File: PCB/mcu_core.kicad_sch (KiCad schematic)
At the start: 24 parts, among them X1 12MHz

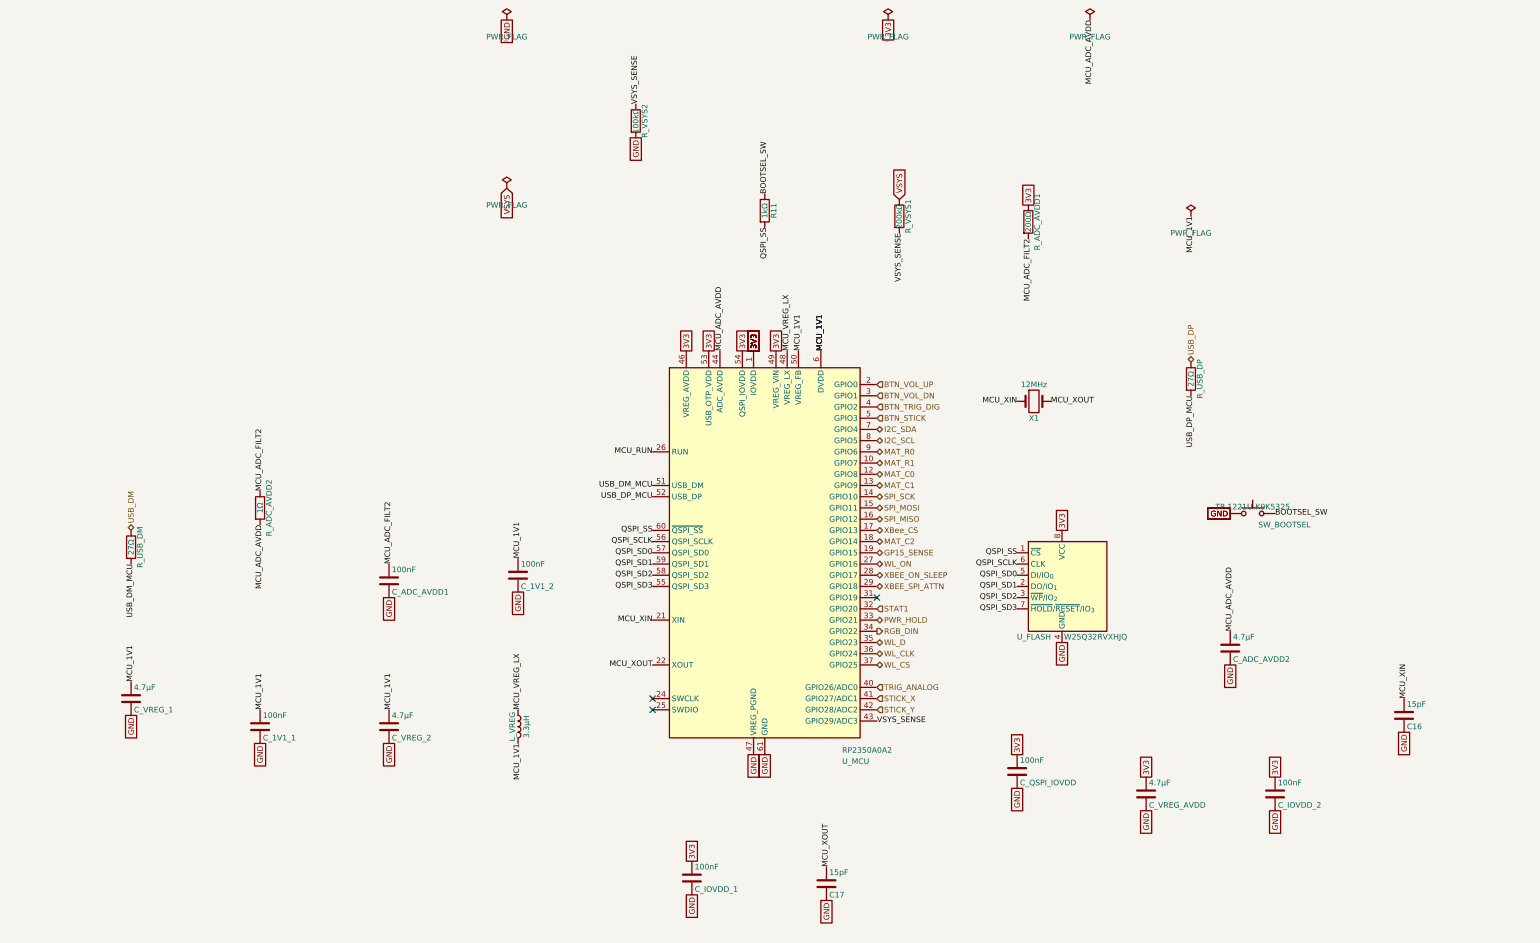
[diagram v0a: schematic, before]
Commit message: refactor: erc is clean
This gets the schematic as clean as it can be.
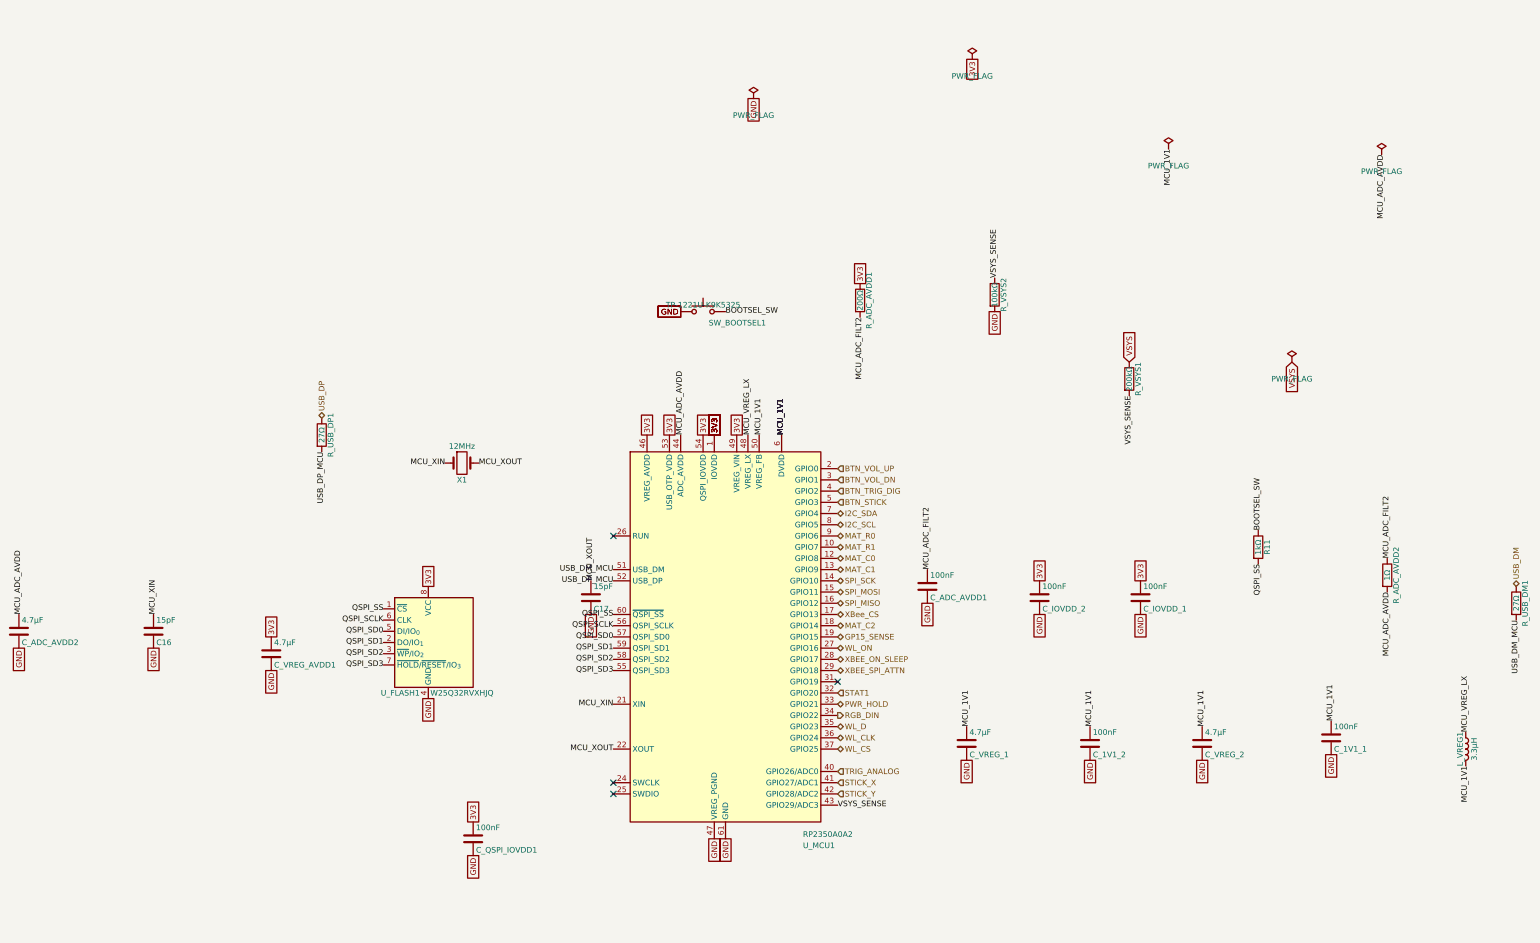
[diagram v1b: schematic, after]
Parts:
- removed C_QSPI_IOVDD: 100nF, symbol Device:C
- removed C_VREG_AVDD: 4.7µF, symbol Device:C
- removed L_VREG: 3.3µH, symbol Device:L
- removed R_USB_DM, R_USB_DP: 27Ω, symbol Device:R
- removed SW_BOOTSEL: TP-1221U-K9K5325, symbol Switch:SW_Push
- removed U_FLASH: W25Q32RVXHJQ, Package_SO:SOIC-8_5.3x5.3mm_P1.27mm, symbol Memory_Flash:W25Q32JVSS
- removed U_MCU: RP2350A0A2, Package_DFN_QFN:QFN-60-1EP_7x7mm_P0.4mm_EP3.4x3.4mm, symbol MCU_RaspberryPi:RP2350A
- added C_QSPI_IOVDD1: 100nF, symbol Device:C
- added C_VREG_AVDD1: 4.7µF, symbol Device:C
- added L_VREG1: 3.3µH, symbol Device:L
- added R_USB_DM1, R_USB_DP1: 27Ω, symbol Device:R
- added SW_BOOTSEL1: TP-1221U-K9K5325, symbol Switch:SW_Push
- added U_FLASH1: W25Q32RVXHJQ, Package_SO:SOIC-8_5.3x5.3mm_P1.27mm, symbol Memory_Flash:W25Q32JVSS
- added U_MCU1: RP2350A0A2, Package_DFN_QFN:QFN-60-1EP_7x7mm_P0.4mm_EP3.4x3.4mm, symbol MCU_RaspberryPi:RP2350A
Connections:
- net 3V3: now also C_QSPI_IOVDD1.1, C_VREG_AVDD1.1, U_FLASH1.8 (VCC), U_MCU1.1 (IOVDD), U_MCU1.11 (IOVDD), U_MCU1.20 (IOVDD), U_MCU1.30 (IOVDD), U_MCU1.38 (IOVDD), U_MCU1.45 (IOVDD), U_MCU1.46 (VREG_AVDD), U_MCU1.49 (VREG_VIN), U_MCU1.53 (USB_OTP_VDD), U_MCU1.54 (QSPI_IOVDD)
- net BOOTSEL_SW: now also SW_BOOTSEL1.2
- net BTN_STICK: now also U_MCU1.5 (GPIO3)
- net BTN_TRIG_DIG: now also U_MCU1.4 (GPIO2)
- net BTN_VOL_DN: now also U_MCU1.3 (GPIO1)
- net BTN_VOL_UP: now also U_MCU1.2 (GPIO0)
- net GND: now also C_QSPI_IOVDD1.2, C_VREG_AVDD1.2, SW_BOOTSEL1.1, U_FLASH1.4 (GND), U_MCU1.47 (VREG_PGND), U_MCU1.61 (GND)
- net GP15_SENSE: now also U_MCU1.19 (GPIO15)
- net I2C_SCL: now also U_MCU1.8 (GPIO5)
- net I2C_SDA: now also U_MCU1.7 (GPIO4)
- net MAT_C0: now also U_MCU1.12 (GPIO8)
- net MAT_C1: now also U_MCU1.13 (GPIO9)
- net MAT_C2: now also U_MCU1.18 (GPIO14)
- net MAT_R0: now also U_MCU1.9 (GPIO6)
- net MAT_R1: now also U_MCU1.10 (GPIO7)
- net MCU_1V1: now also L_VREG1.2, U_MCU1.23 (DVDD), U_MCU1.39 (DVDD), U_MCU1.50 (VREG_FB), U_MCU1.6 (DVDD)
- net MCU_ADC_AVDD: now also U_MCU1.44 (ADC_AVDD)
- net MCU_VREG_LX: now also L_VREG1.1, U_MCU1.48 (VREG_LX)
- net MCU_XIN: now also U_MCU1.21 (XIN)
- net MCU_XOUT: now also U_MCU1.22 (XOUT)
- net PWR_HOLD: now also U_MCU1.33 (GPIO21)
- net QSPI_SCLK: now also U_FLASH1.6 (CLK), U_MCU1.56 (QSPI_SCLK)
- net QSPI_SD0: now also U_FLASH1.5 (DI/IO_{0}), U_MCU1.57 (QSPI_SD0)
- net QSPI_SD1: now also U_FLASH1.2 (DO/IO_{1}), U_MCU1.59 (QSPI_SD1)
- net QSPI_SD2: now also U_FLASH1.3 (~{WP}/IO_{2}), U_MCU1.58 (QSPI_SD2)
- net QSPI_SD3: now also U_FLASH1.7 (~{HOLD}/~{RESET}/IO_{3}), U_MCU1.55 (QSPI_SD3)
- net QSPI_SS: now also U_FLASH1.1 (~{CS}), U_MCU1.60 (~{QSPI_SS})
- net RGB_DIN: now also U_MCU1.34 (GPIO22)
- net SPI_MISO: now also U_MCU1.16 (GPIO12)
- net SPI_MOSI: now also U_MCU1.15 (GPIO11)
- net SPI_SCK: now also U_MCU1.14 (GPIO10)
- net STAT1: now also U_MCU1.32 (GPIO20)
- net STICK_X: now also U_MCU1.41 (GPIO27/ADC1)
- net STICK_Y: now also U_MCU1.42 (GPIO28/ADC2)
- net TRIG_ANALOG: now also U_MCU1.40 (GPIO26/ADC0)
- net USB_DM: now also R_USB_DM1.1
- net USB_DM_MCU: now also R_USB_DM1.2, U_MCU1.51 (USB_DM)
- net USB_DP: now also R_USB_DP1.1
- net USB_DP_MCU: now also R_USB_DP1.2, U_MCU1.52 (USB_DP)
- net VSYS_SENSE: now also U_MCU1.43 (GPIO29/ADC3)
- net WL_CLK: now also U_MCU1.36 (GPIO24)
- net WL_CS: now also U_MCU1.37 (GPIO25)
- net WL_D: now also U_MCU1.35 (GPIO23)
- net WL_ON: now also U_MCU1.27 (GPIO16)
- net XBEE_ON_SLEEP: now also U_MCU1.28 (GPIO17)
- net XBEE_SPI_ATTN: now also U_MCU1.29 (GPIO18)
- net XBee_CS: now also U_MCU1.17 (GPIO13)
- no-connect marks 3 -> 4

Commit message: refactor: switch over to esp32-s3-wroom1 (#13)
This refactors to the esp32-s3 to avoid every problem we encountered with the raspberry pi options.
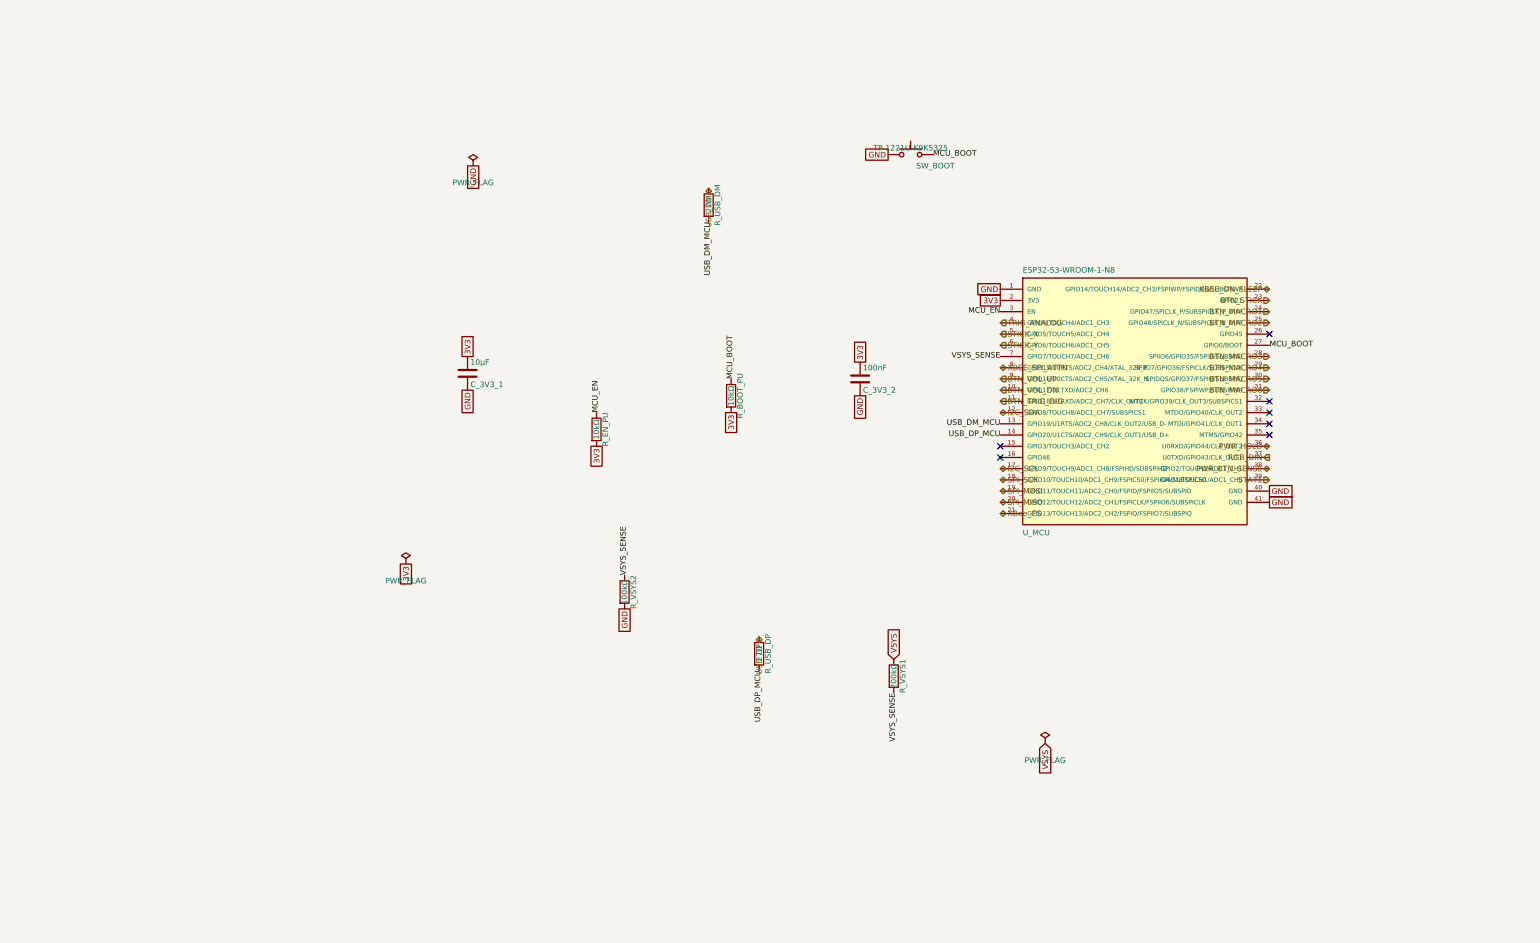
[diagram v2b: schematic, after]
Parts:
- removed C16, C17: 15pF, symbol Device:C
- removed C_1V1_1, C_1V1_2, C_ADC_AVDD1, C_IOVDD_1, C_IOVDD_2, C_QSPI_IOVDD1: 100nF, symbol Device:C
- removed C_ADC_AVDD2, C_VREG_1, C_VREG_2, C_VREG_AVDD1: 4.7µF, symbol Device:C
- removed L_VREG1: 3.3µH, symbol Device:L
- removed R11: 1kΩ, symbol Device:R
- removed R_ADC_AVDD1: 200Ω, symbol Device:R
- removed R_ADC_AVDD2: 1Ω, symbol Device:R
- removed R_USB_DM1, R_USB_DP1: 27Ω, symbol Device:R
- removed SW_BOOTSEL1: TP-1221U-K9K5325, symbol Switch:SW_Push
- removed U_FLASH1: W25Q32RVXHJQ, Package_SO:SOIC-8_5.3x5.3mm_P1.27mm, symbol Memory_Flash:W25Q32JVSS
- removed U_MCU1: RP2350A0A2, Package_DFN_QFN:QFN-60-1EP_7x7mm_P0.4mm_EP3.4x3.4mm, symbol MCU_RaspberryPi:RP2350A
- removed X1: 12MHz, symbol Device:Crystal
- added C_3V3_1: 10µF, Capacitor_SMD:C_0603_1608Metric, symbol Device:C
- added C_3V3_2: 100nF, Capacitor_SMD:C_0402_1005Metric, symbol Device:C
- added PF_3V3, PF_GND, PF_VSYS: PWR_FLAG, symbol power:PWR_FLAG
- added R_BOOT_PU, R_EN_PU: 10kΩ, Resistor_SMD:R_0402_1005Metric, symbol Device:R
- added R_USB_DM, R_USB_DP: 27Ω, Resistor_SMD:R_0402_1005Metric, symbol Device:R
- added SW_BOOT: TP-1221U-K9K5325, Button_Switch_SMD:SW_SPST_TL3342, symbol Switch:SW_Push
- added U_MCU: ESP32-S3-WROOM-1-N8, Espressif:ESP32-S3-WROOM-1, symbol Espressif:ESP32-S3-WROOM-1
- R_VSYS1, R_VSYS2: footprint (none) -> Resistor_SMD:R_0402_1005Metric
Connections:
- net 3V3: now also C_3V3_1.1, C_3V3_2.1, PF_3V3.1, R_BOOT_PU.2, R_EN_PU.2, U_MCU.2 (3V3)
- net BTN_STICK: now also U_MCU.23 (GPIO21)
- net BTN_TRIG_DIG: now also U_MCU.11 (GPIO18/U1RXD/ADC2_CH7/CLK_OUT3)
- net BTN_VOL_DN: now also U_MCU.10 (GPIO17/U1TXD/ADC2_CH6)
- net BTN_VOL_UP: now also U_MCU.9 (GPIO16/U0CTS/ADC2_CH5/XTAL_32K_N)
- net GND: now also C_3V3_1.2, C_3V3_2.2, PF_GND.1, SW_BOOT.1, U_MCU.1 (GND), U_MCU.40 (GND), U_MCU.41 (GND)
- net I2C_SCL: now also U_MCU.17 (GPIO9/TOUCH9/ADC1_CH8/FSPIHD/SUBSPIHD)
- net I2C_SDA: now also U_MCU.12 (GPIO8/TOUCH8/ADC1_CH7/SUBSPICS1)
- net PWR_HOLD: now also U_MCU.36 (U0RXD/GPIO44/CLK_OUT2)
- net RGB_DIN: now also U_MCU.37 (U0TXD/GPIO43/CLK_OUT1)
- net SPI_MISO: now also U_MCU.20 (GPIO12/TOUCH12/ADC2_CH1/FSPICLK/FSPIIO6/SUBSPICLK)
- net SPI_MOSI: now also U_MCU.19 (GPIO11/TOUCH11/ADC2_CH0/FSPID/FSPIIO5/SUBSPID)
- net SPI_SCK: now also U_MCU.18 (GPIO10/TOUCH10/ADC1_CH9/FSPICS0/FSPIIO4/SUBSPICS0)
- net STAT1: now also U_MCU.39 (GPIO1/TOUCH1/ADC1_CH0)
- net STICK_X: now also U_MCU.5 (GPIO5/TOUCH5/ADC1_CH4)
- net STICK_Y: now also U_MCU.6 (GPIO6/TOUCH6/ADC1_CH5)
- net TRIG_ANALOG: now also U_MCU.4 (GPIO4/TOUCH4/ADC1_CH3)
- net USB_DM: now also R_USB_DM.1
- net USB_DM_MCU: now also R_USB_DM.2, U_MCU.13 (GPIO19/U1RTS/ADC2_CH8/CLK_OUT2/USB_D-)
- net USB_DP: now also R_USB_DP.1
- net USB_DP_MCU: now also R_USB_DP.2, U_MCU.14 (GPIO20/U1CTS/ADC2_CH9/CLK_OUT1/USB_D+)
- net VSYS: now also PF_VSYS.1
- net VSYS_SENSE: now also U_MCU.7 (GPIO7/TOUCH7/ADC1_CH6)
- net XBEE_ON_SLEEP: now also U_MCU.22 (GPIO14/TOUCH14/ADC2_CH3/FSPIWP/FSPIDQS/SUBSPIWP)
- net XBEE_SPI_ATTN: now also U_MCU.8 (GPIO15/U0RTS/ADC2_CH4/XTAL_32K_P)
- net XBee_CS: now also U_MCU.21 (GPIO13/TOUCH13/ADC2_CH2/FSPIQ/FSPIIO7/SUBSPIQ)
- new net BTN_MACRO1: U_MCU.24 (GPIO47/SPICLK_P/SUBSPICLK_P_DIFF)
- new net BTN_MACRO2: U_MCU.25 (GPIO48/SPICLK_N/SUBSPICLK_N_DIFF)
- new net BTN_MACRO3: U_MCU.28 (SPIIO6/GPIO35/FSPID/SUBSPID)
- new net BTN_MACRO4: U_MCU.29 (SPIIO7/GPIO36/FSPICLK/SUBSPICLK)
- new net BTN_MACRO5: U_MCU.30 (SPIDQS/GPIO37/FSPIQ/SUBSPIQ)
- new net BTN_MACRO6: U_MCU.31 (GPIO38/FSPIWP/SUBSPIWP)
- new net MCU_BOOT: R_BOOT_PU.1, SW_BOOT.2, U_MCU.27 (GPIO0/BOOT)
- new net MCU_EN: R_EN_PU.1, U_MCU.3 (EN)
- new net PWR_BTN_SENSE: U_MCU.38 (GPIO2/TOUCH2/ADC1_CH1)
- no-connect marks 4 -> 7
